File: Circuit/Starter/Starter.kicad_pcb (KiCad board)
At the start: 2 copper layers, 215.9 x 132.1 mm, 18 parts, among them J1 From Power, J2 Output+, J3 Output-, T1 BSH12-N406L 8:6400, T2 20:20, T3 20:20

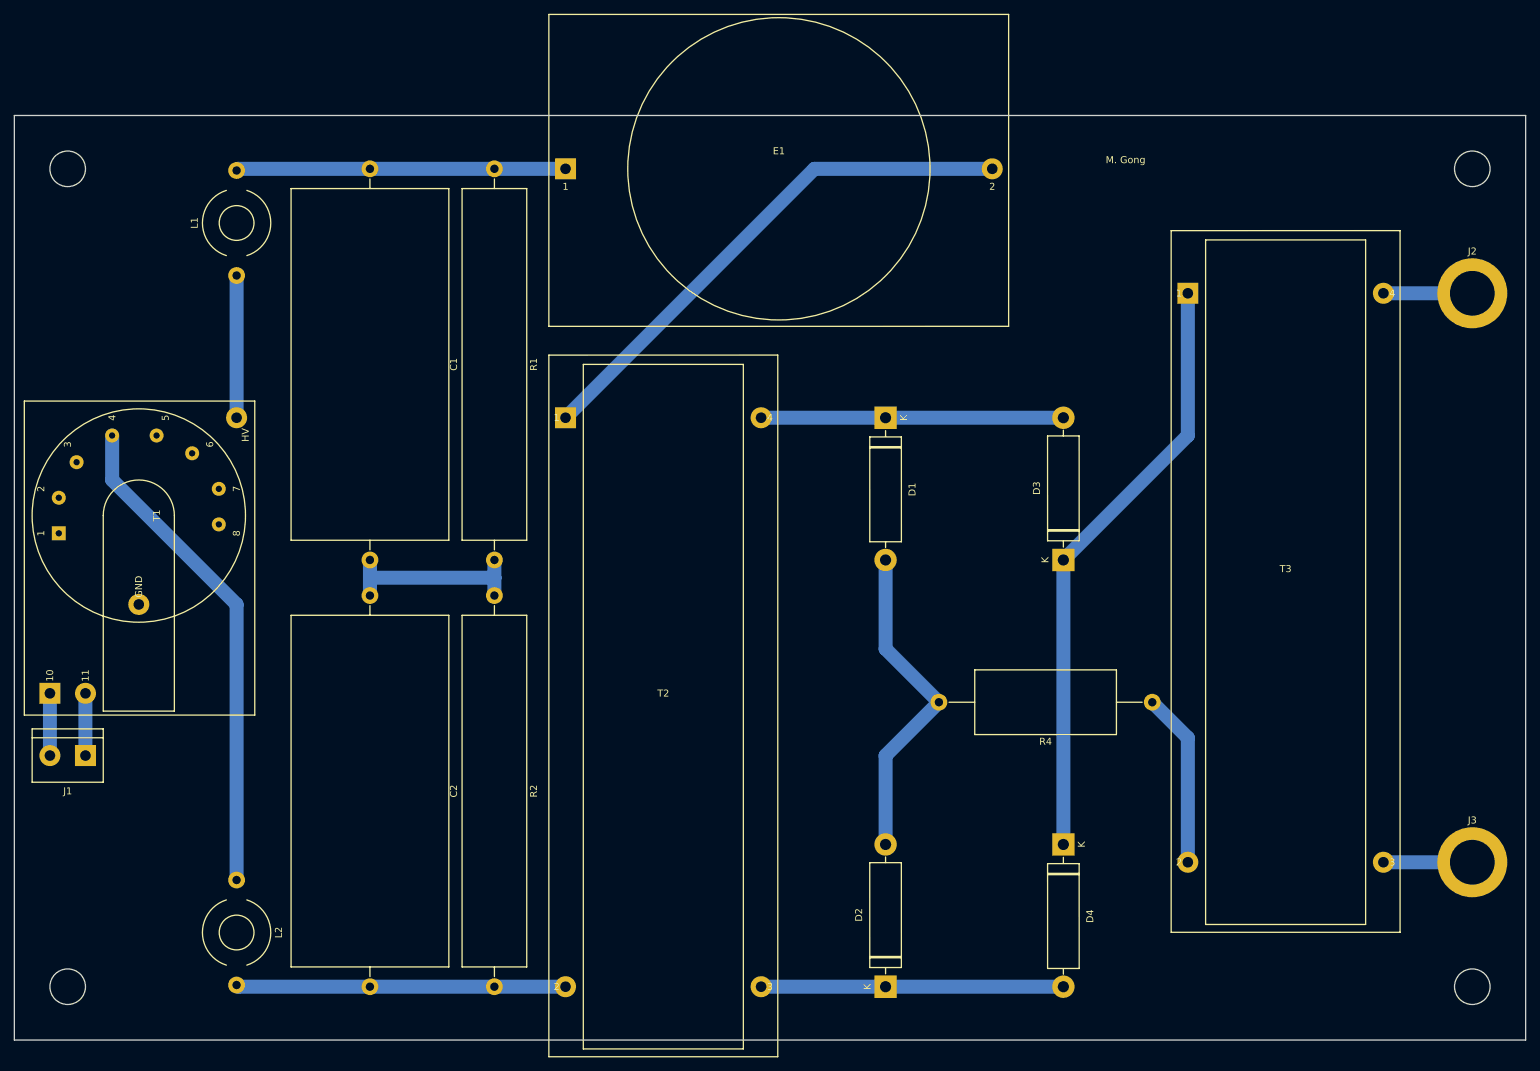
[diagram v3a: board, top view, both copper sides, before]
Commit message: [Circuit] Remove the full bridge from the output side of the starter, then change the capacitor bank to non-polarized configuration
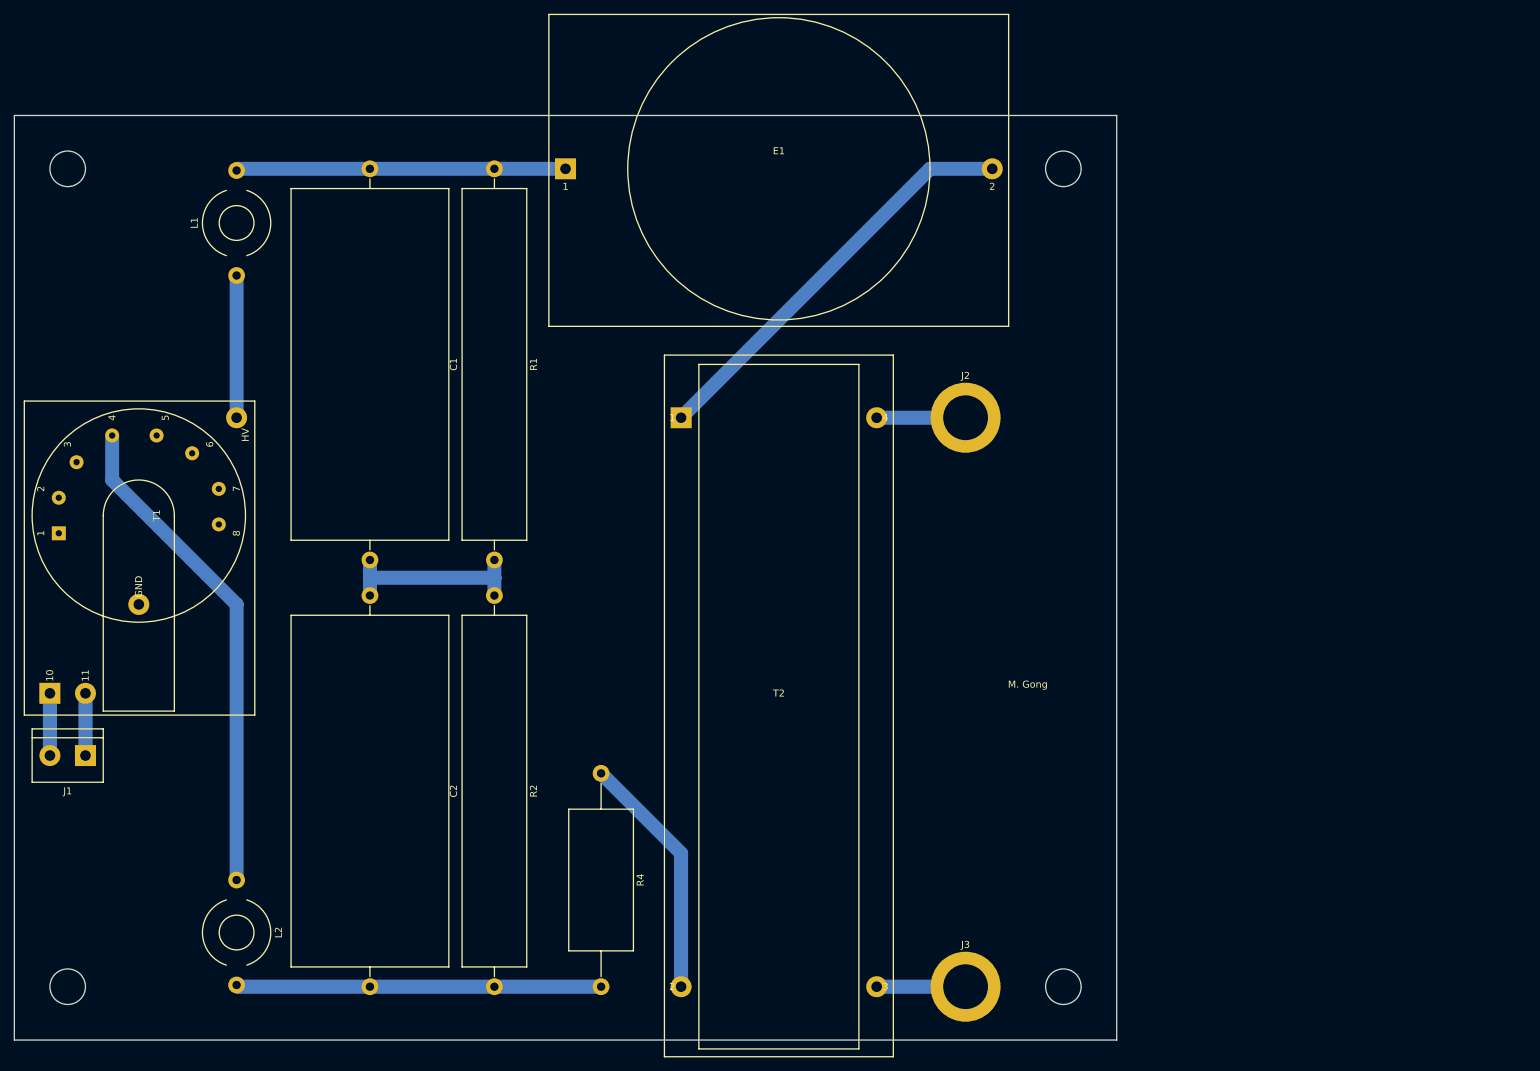
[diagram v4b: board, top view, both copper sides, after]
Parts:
- removed D1, D2, D3, D4: 2CL2FM, Power:Diode_2CL_Horizontal
- removed the T2 at (119.4, 73.7)
- moved R4 79.4 mm to (124.5, 124.5), turned to 270 degrees
- moved T2 74.5 mm to (135.9, 73.7)
- moved J3 74.5 mm to (176.5, 154.9)
- moved J2 74.5 mm to (176.5, 73.7)
- renumbered T3 to T2
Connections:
- net /Output+ renamed /PowerOut+
- net /Output- renamed /PowerOut-
- R4 pad 2: Net-(D1-Pad2) -> Net-(C2-Pad2)
- T2 pad 1: Net-(D3-Pad1) -> Net-(E1-Pad2)
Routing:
- net Net-(D3-Pad1): track 86.1 -> 0.00 mm
- net Net-(D1-Pad2): track 47.0 -> 0.00 mm
- net Net-(D2-Pad1): track 43.2 -> 0.00 mm
- net Net-(D1-Pad1): track 43.2 -> 0.00 mm
- net Net-(E1-Pad2): track 75.7 -> 59.2 mm
- net Net-(R4-Pad1): track 25.0 -> 35.2 mm
- net Net-(C2-Pad2): track 47.1 -> 52.2 mm
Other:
- board size 215.9 x 132.1 mm -> 157.5 x 132.1 mm

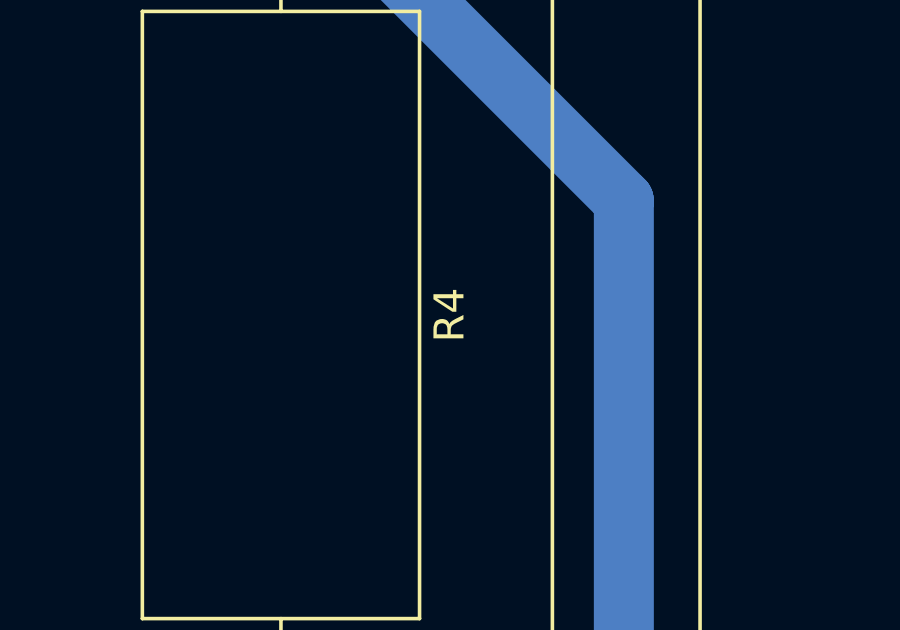
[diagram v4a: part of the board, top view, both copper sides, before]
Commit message: [Circuit] Fix the reference of a resistor in starter module
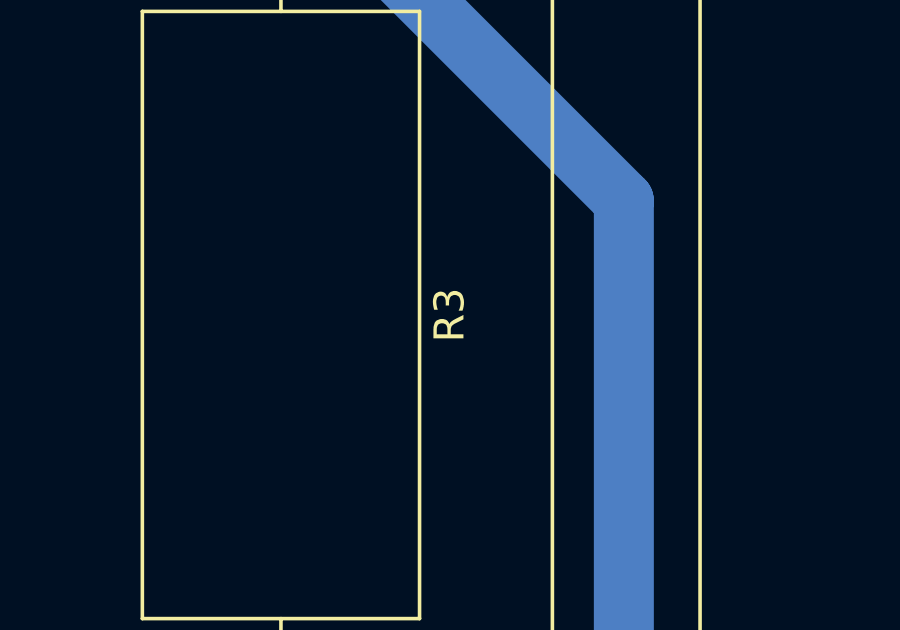
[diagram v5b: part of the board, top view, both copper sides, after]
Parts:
- renumbered R4 to R3
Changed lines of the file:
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@@
   (net 5 /PowerIn-)
   (net 6 /PowerIn+)
-  (net 7 "Net-(R4-Pad1)")
-  (net 8 "Net-(L1-Pad1)")
-  (net 9 "Net-(L2-Pad1)")
-  (net 10 /PowerOut+)
-  (net 11 /PowerOut-)
+  (net 7 "Net-(L1-Pad1)")
+  (net 8 "Net-(L2-Pad1)")
+  (net 9 /PowerOut+)
+  (net 10 /PowerOut-)
+  (net 11 "Net-(R3-Pad1)")
   (net_class Default "This is the default net class."
     (clearance 0.2)
@@
     (add_net "Net-(L1-Pad1)")
     (add_net "Net-(L2-Pad1)")
-    (add_net "Net-(R4-Pad1)")
+    (add_net "Net-(R3-Pad1)")
   )
   (module Resistor_THT:R_Axial_DIN0922_L20.0mm_D9.0mm_P30.48mm_Horizontal (layer F.Cu)
@@
     (descr "Resistor, Axial_DIN0922 series, Axial, Horizontal, pin pitch=30.48mm, 5W, length*diameter=20*9mm^2, http://www.vishay.com/docs/20128/wkxwrx.pdf")
     (tags "Resistor Axial_DIN0922 series Axial Horizontal pin pitch 30.48mm 5W length 20mm diameter 9mm")
-    (fp_text reference R4 (at 15.24 -5.62 90) (layer F.SilkS)
+    (fp_text reference R3 (at 15.24 -5.62 90) (layer F.SilkS)
       (effects (font (size 1 1) (thickness 0.15)))
     )
@@
       (net 3 "Net-(C2-Pad2)"))
     (pad 1 thru_hole circle (at 0 0 270) (size 2.4 2.4) (drill 1.2) (layers *.Cu *.Mask)
-      (net 7 "Net-(R4-Pad1)"))
+      (net 11 "Net-(R3-Pad1)"))
     (model ${KISYS3DMOD}/Resistor_THT.3dshapes/R_Axial_DIN0922_L20.0mm_D9.0mm_P30.48mm_Horizontal.wrl
       (at (xyz 0 0 0))
@@
     )
     (pad 1 thru_hole circle (at 0 0) (size 10 10) (drill 6.4) (layers *.Cu *.Mask)
-      (net 11 /PowerOut-))
+      (net 10 /PowerOut-))
   )
   (module MountingHole:MountingHole_6.4mm_M6_ISO14580_Pad (layer F.Cu)
@@
     )
     (pad 1 thru_hole circle (at 0 0) (size 10 10) (drill 6.4) (layers *.Cu *.Mask)
-      (net 10 /PowerOut+))
+      (net 9 /PowerOut+))
   )
   (module Power:Flyback_Transformer_BSH12-N406L (layer F.Cu)
@@
       (net 6 /PowerIn+))
     (pad 12 thru_hole circle (at 0 0 270) (size 3 3) (drill 1.52) (layers *.Cu *.Mask)
-      (net 8 "Net-(L1-Pad1)"))
+      (net 7 "Net-(L1-Pad1)"))
     (pad 9 thru_hole circle (at 26.67 13.97 270) (size 3 3) (drill 1.52) (layers *.Cu *.Mask))
     (pad 8 thru_hole circle (at 15.24 2.54 270) (size 2 2) (drill 0.9) (layers *.Cu *.Mask))
@@
     (pad 2 thru_hole circle (at 11.43 25.4 270) (size 2 2) (drill 0.9) (layers *.Cu *.Mask))
     (pad 4 thru_hole circle (at 2.54 17.78 270) (size 2 2) (drill 0.9) (layers *.Cu *.Mask)
-      (net 9 "Net-(L2-Pad1)"))
+      (net 8 "Net-(L2-Pad1)"))
     (pad 5 thru_hole circle (at 2.54 11.43 270) (size 2 2) (drill 0.9) (layers *.Cu *.Mask))
     (pad 3 thru_hole circle (at 6.35 22.86 270) (size 2 2) (drill 0.9) (layers *.Cu *.Mask))
@@
       (net 4 "Net-(E1-Pad2)"))
     (pad 2 thru_hole circle (at 0 81.28) (size 3 3) (drill 1.52) (layers *.Cu *.Mask)
-      (net 7 "Net-(R4-Pad1)"))
+      (net 11 "Net-(R3-Pad1)"))
     (pad 4 thru_hole circle (at 27.94 0) (size 3 3) (drill 1.52) (layers *.Cu *.Mask)
-      (net 10 /PowerOut+))
+      (net 9 /PowerOut+))
     (pad 3 thru_hole circle (at 27.94 81.28) (size 3 3) (drill 1.52) (layers *.Cu *.Mask)
-      (net 11 /PowerOut-))
+      (net 10 /PowerOut-))
   )
   (module Inductor_THT:L_Toroid_Horizontal_D9.5mm_P15.00mm_Diameter10-5mm_Amidon-T37 (layer F.Cu)
@@
     )
     (pad 1 thru_hole circle (at 0 0 270) (size 2.4 2.4) (drill 1.2) (layers *.Cu *.Mask)
-      (net 9 "Net-(L2-Pad1)"))
+      (net 8 "Net-(L2-Pad1)"))
     (pad 2 thru_hole circle (at 15 0 270) (size 2.4 2.4) (drill 1.2) (layers *.Cu *.Mask)
       (net 3 "Net-(C2-Pad2)"))
@@
       (net 1 "Net-(C1-Pad1)"))
     (pad 1 thru_hole circle (at 0 0 90) (size 2.4 2.4) (drill 1.2) (layers *.Cu *.Mask)
-      (net 8 "Net-(L1-Pad1)"))
+      (net 7 "Net-(L1-Pad1)"))
     (model ${KISYS3DMOD}/Inductor_THT.3dshapes/L_Toroid_Horizontal_D9.5mm_P15.00mm_Diameter10-5mm_Amidon-T37.wrl
       (at (xyz 0 0 0))
@@
   (segment (start 50.8 113.03) (end 50.8 121.92) (width 2) (layer B.Cu) (net 5) (status 30))
   (segment (start 45.72 113.03) (end 45.72 121.92) (width 2) (layer B.Cu) (net 6) (status 30))
-  (segment (start 135.89 135.89) (end 124.46 124.46) (width 2) (layer B.Cu) (net 7))
-  (segment (start 135.89 154.94) (end 135.89 135.89) (width 2) (layer B.Cu) (net 7))
-  (segment (start 163.83 73.66) (end 176.53 73.66) (width 2) (layer B.Cu) (net 10) (status 30))
-  (segment (start 163.83 154.94) (end 176.53 154.94) (width 2) (layer B.Cu) (net 11) (status 30))
-  (segment (start 72.39 73.66) (end 72.39 53.34) (width 2) (layer B.Cu) (net 8) (status 30))
-  (segment (start 54.61 76.2) (end 54.61 82.55) (width 2) (layer B.Cu) (net 9) (status 10))
-  (segment (start 72.39 139.7) (end 72.39 100.33) (width 2) (layer B.Cu) (net 9) (status 10))
-  (segment (start 54.61 82.55) (end 72.39 100.33) (width 2) (layer B.Cu) (net 9))
+  (segment (start 135.89 135.89) (end 124.46 124.46) (width 2) (layer B.Cu) (net 11))
+  (segment (start 135.89 154.94) (end 135.89 135.89) (width 2) (layer B.Cu) (net 11))
+  (segment (start 72.39 73.66) (end 72.39 53.34) (width 2) (layer B.Cu) (net 7) (status 30))
+  (segment (start 54.61 76.2) (end 54.61 82.55) (width 2) (layer B.Cu) (net 8) (status 10))
+  (segment (start 72.39 139.7) (end 72.39 100.33) (width 2) (layer B.Cu) (net 8) (status 10))
+  (segment (start 54.61 82.55) (end 72.39 100.33) (width 2) (layer B.Cu) (net 8))
+  (segment (start 163.83 73.66) (end 176.53 73.66) (width 2) (layer B.Cu) (net 9) (status 30))
+  (segment (start 163.83 154.94) (end 176.53 154.94) (width 2) (layer B.Cu) (net 10) (status 30))
 )

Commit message: [Circuit] Upgrade to KiCad 6 format
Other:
- net class Default removed
